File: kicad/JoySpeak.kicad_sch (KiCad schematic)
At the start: 61 parts, among them CN1 AUDIO_IN, CN2 AUDIO_OUT, J1 Hexpansion-Connector, J3 Conn_01x02_Pin, J4 Conn_01x01_Pin, J5 Conn_01x02_Pin, SW1 TS-1187A-B-A-B, SW2 TS-1187A-B-A-B, U1 TLV320AIC3100, U2 YV13S-L7.85-B10KA(60)-0-DL01, U3 RP2040-ZERO, U4 AMS1117-1.8

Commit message: Closing in - commiting before adding teardrops
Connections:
- net AUD_BCLK: now also U3.9 (GP8); no longer U3.11 (GP10)
- net AUD_DIN: now also U3.12 (GP11); no longer U3.14 (GP13)
- net AUD_DOUT: now also U3.11 (GP10); no longer U3.13 (GP12)
- net AUD_I2C0_SCL: now also R2.2; no longer R3.2
- net AUD_I2C0_SDA: now also R3.2; no longer R2.2
- net AUD_MCLK: now also U3.8 (GP7); no longer U3.15 (GP14)
- net AUD_WCLK: now also U3.10 (GP9); no longer U3.12 (GP11)
- net BUTTON_1: now also U3.1 (GP0); no longer U3.20 (GP29)
- net BUTTON_2: now also U3.2 (GP1); no longer U3.19 (GP28)
- net HEX_HS_F: now also U3.7 (GP6); no longer U3.2 (GP1)
- net HEX_I2C1_SCL: now also U3.4 (GP3); no longer U3.8 (GP7)
- net HEX_I2C1_SDA: now also U3.3 (GP2); no longer U3.7 (GP6)
- net JACK_IN_DETECT: now also U3.16 (GP15); no longer U3.3 (GP2)
- net JACK_OUT_DETECT: now also U3.15 (GP14); no longer U3.4 (GP3)
- net JOY_BUT: now also U3.19 (GP28); no longer U3.1 (GP0)
- net LEDS_DIN: now also U3.14 (GP13); no longer U3.10 (GP9)
- net PJON_DATA: now also U3.20 (GP29); no longer U3.16 (GP15)
- net RESETN: now also U3.13 (GP12); no longer U3.9 (GP8)
- net JOY_ADC0 renamed JOY_V
- net JOY_V: now also JP1.2 (B), R7.1; no longer R8.2
- net JOY_ADC1 renamed JOY_H
- net JOY_H: now also R8.2; no longer JP1.2 (B), R7.1
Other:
- note added: "Check it's mappable!"
- note added: "Default to left?"
- moved on the sheet: C37, C41, C42, LED1, LED2, R1, R4, R5, R9, U3

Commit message: Committing before flipping RJ45 connector
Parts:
- CN1, CN2: LCSC C5155561 -> C49284725
- J3, J5: now left out of the parts list
- JP2, JP3, JP4, JP5: LCSC (none) -> C32713269; now in the parts list
- LS1: now in the parts list
- U1: footprint Package_DFN_QFN:VQFN-32-1EP_5x5mm_P0.5mm_EP3.5x3.5mm -> Package_DFN_QFN:VQFN-32-1EP_5x5mm_P0.5mm_EP3.5x3.5mm_ThermalVias
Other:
- moved on the sheet: C41, C42, R2, R3, R4, R5, R9, U3

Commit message: Committing before attempting 4-layer layout
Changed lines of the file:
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@@
 		)
 	)
-	(text_box "Separate ground planes?\nLCSC BOM - add screws 2mm?, nuts\nCheck LCSC quantities\nCheck LCSC + JLC order together\nBuy RP2040s\nDouble check RP2040 cutout\nGo PCBA to confirm chip placement\n"
+	(text_box "Separate ground planes?\nBuy RP2040s on Ali\nDouble check RP2040 cutout\nSimplify silkscreening to values\nDFM check\nLCSC BOM - added standoffs, no screws\nAdd spares to JLC quantities\nCheck LCSC + JLC order together\n$176.78"
 		(exclude_from_sim no)
-		(at 289.56 55.88 0)
-		(size 76.2 16.2161)
+		(at 289.56 55.8947 0)
+		(size 43.18 20.3053)
 		(margins 0.9525 0.9525 0.9525 0.9525)
 		(stroke
@@
 	(text_box "# Networking: 2 modes\n\nStar (Installation mode): In this configuration, no USB cables are used. You have a heavy-duty central 5V power supply inside a distributor box. The box has a permanent $1\\text{ k}\\Omega$ resistor across its central data knot. 40-meter total radiating lines run out to each node using standard Ethernet cables.\n\nDaisy-Chain (Desktop mode): Use 2-wire cables (Data/GND only; 5V is disconnected to prevent backfeeding). Each node powers itself via USB. Plug a \"Terminator Plug\" (a loose RJ45 with a 4.7kΩ resistor between Pin 4 and GND) into any open jack at the end of the chain."
 		(exclude_from_sim no)
-		(at 213.36 -20.8638 0)
-		(size 88.9 28.4838)
+		(at 210.82 -17.78 0)
+		(size 88.9 24.3946)
 		(margins 0.9525 0.9525 0.9525 0.9525)
 		(stroke
@@
 	(text_box "240	10uF							C33546013\n280	100nF							C24497\n40	AUDIO_IN/OUT					C49284725\n40	BLM21PG221SN1D					C85840\n40	SK6812MINI-EA					C5378731\n20	MSM381ACB026					C51928208\n60	470R							C2933707 \n100	4.7k							C2907387 \n20	47k								C2933708 \n20	HC-RJ45-5JA-2-6-S				C5341200\n40	TS-1187A-B-A-B					C318884\n20	TLV320AIC3100					C478458\n20	YV13S-L7.85-B10KA(60)-0-DL01	C37323747\n20	AMS1117-1.8						C347220\n20	Speaker							C50387235\n80	RP2040_VOLTAGE_JUMPER			C32713269\n80 	Shunt jumpers					C5305\n\n+ 10%\n\n264	10uF							C33546013\n308	100nF							C24497\n44	AUDIO_IN/OUT					C49284725\n44	BLM21PG221SN1D					C85840\n44	SK6812MINI-EA					C5378731\n22	MSM381ACB026					C51928208\n66	470R							C2933707 \n110	4.7k							C2907387 \n22	47k								C2933708 \n22	HC-RJ45-5JA-2-6-S				C5341200\n44	TS-1187A-B-A-B					C318884\n22	TLV320AIC3100					C478458\n22	YV13S-L7.85-B10KA(60)-0-DL01	C37323747\n22	AMS1117-1.8						C347220\n22	Speaker							C50387235\n88	RP2040_VOLTAGE_JUMPER			C32713269\n88 	Shunt jumpers					C5305"
 		(exclude_from_sim no)
-		(at 289.56 93.98 0)
+		(at 289.56 76.2 0)
 		(size 63.5 77.5549)
 		(margins 0.9525 0.9525 0.9525 0.9525)

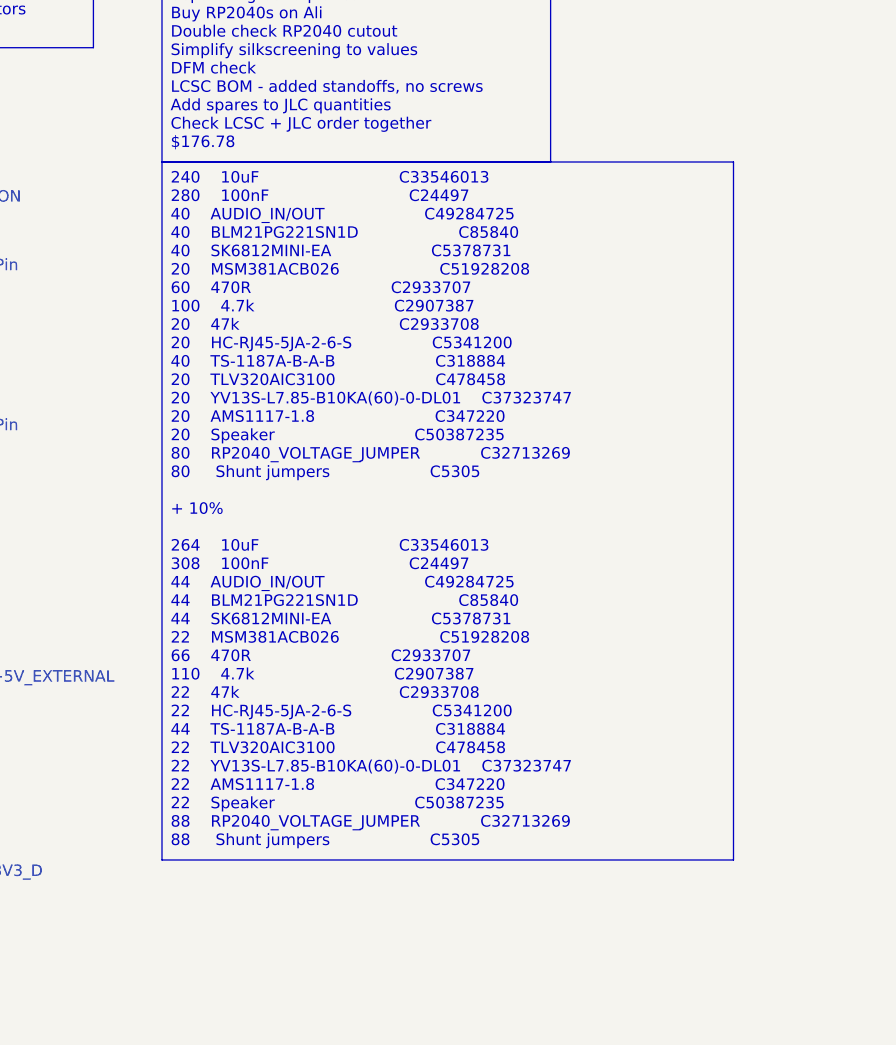
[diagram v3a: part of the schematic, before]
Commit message: Fixed all DRC errors
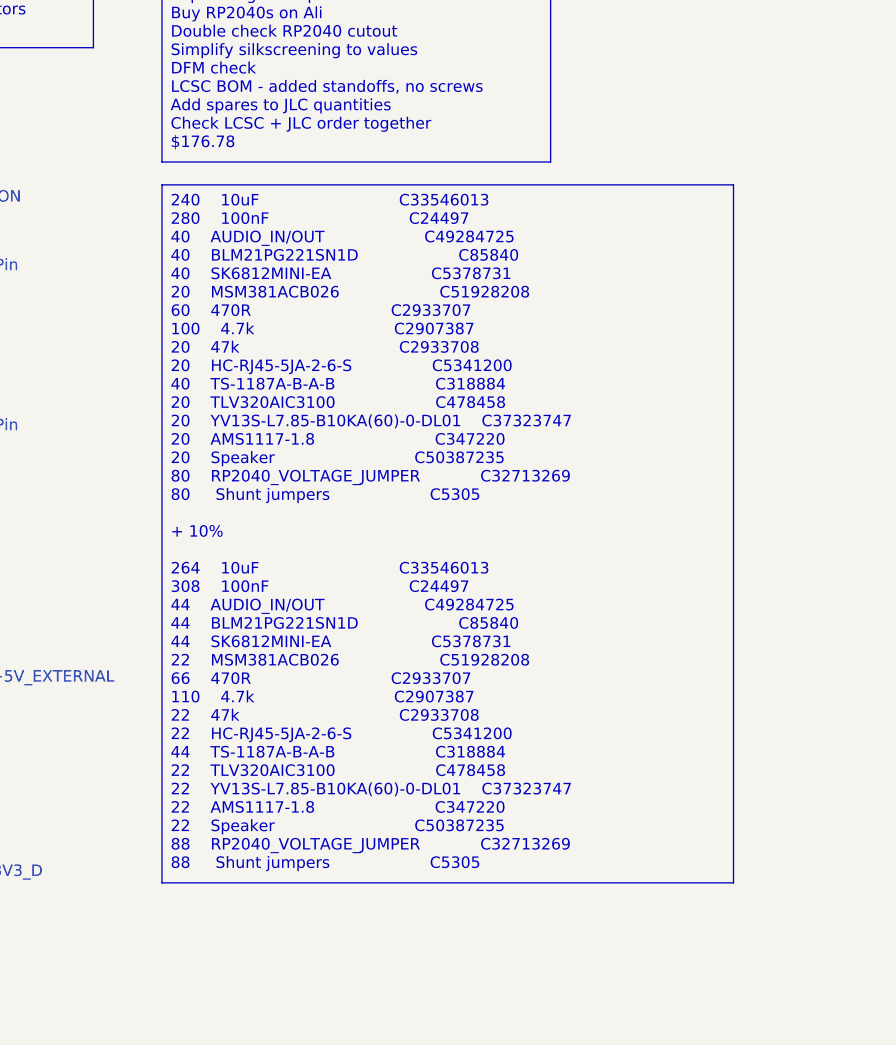
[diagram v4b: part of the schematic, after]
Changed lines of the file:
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@@
 	(text_box "240	10uF							C33546013\n280	100nF							C24497\n40	AUDIO_IN/OUT					C49284725\n40	BLM21PG221SN1D					C85840\n40	SK6812MINI-EA					C5378731\n20	MSM381ACB026					C51928208\n60	470R							C2933707 \n100	4.7k							C2907387 \n20	47k								C2933708 \n20	HC-RJ45-5JA-2-6-S				C5341200\n40	TS-1187A-B-A-B					C318884\n20	TLV320AIC3100					C478458\n20	YV13S-L7.85-B10KA(60)-0-DL01	C37323747\n20	AMS1117-1.8						C347220\n20	Speaker							C50387235\n80	RP2040_VOLTAGE_JUMPER			C32713269\n80 	Shunt jumpers					C5305\n\n+ 10%\n\n264	10uF							C33546013\n308	100nF							C24497\n44	AUDIO_IN/OUT					C49284725\n44	BLM21PG221SN1D					C85840\n44	SK6812MINI-EA					C5378731\n22	MSM381ACB026					C51928208\n66	470R							C2933707 \n110	4.7k							C2907387 \n22	47k								C2933708 \n22	HC-RJ45-5JA-2-6-S				C5341200\n44	TS-1187A-B-A-B					C318884\n22	TLV320AIC3100					C478458\n22	YV13S-L7.85-B10KA(60)-0-DL01	C37323747\n22	AMS1117-1.8						C347220\n22	Speaker							C50387235\n88	RP2040_VOLTAGE_JUMPER			C32713269\n88 	Shunt jumpers					C5305"
 		(exclude_from_sim no)
-		(at 289.56 76.2 0)
+		(at 289.56 78.74 0)
 		(size 63.5 77.5549)
 		(margins 0.9525 0.9525 0.9525 0.9525)
